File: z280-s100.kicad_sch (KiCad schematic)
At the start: 42 parts, among them J10 Config header (3x8), J7 Serial header (2x5), J8 S-100 edge connector (100-pin), J9 JTAG header (1x6), U1 Z280 Z-BUS (12 MHz), U10 AT28C256 (32Kx8), U11 AT28C256 (32Kx8), U12 LM7805, U13 DS1813, U14 MAX232, U15 74HCT245, U16 74HCT245, U17 74HCT245, U18 74HCT245, U19 74HCT245, U2 74HC573, U20 74HCT245, U21 74HCT244, U22 74F138, U23 74F521, U24 74F521, U25 74F245, U26 74F245, U27 LM323K, U3 74HC573, U4 ATF1508AS (PLCC-84), U5 ATF1508AS (PLCC-84), U6 IS61C5128AS-25QLI (512Kx8), U7 IS61C5128AS-25QLI (512Kx8), U8 IS61C5128AS-25QLI (512Kx8), U9 IS61C5128AS-25QLI (512Kx8), Y1 24 MHz, Y2 24 MHz

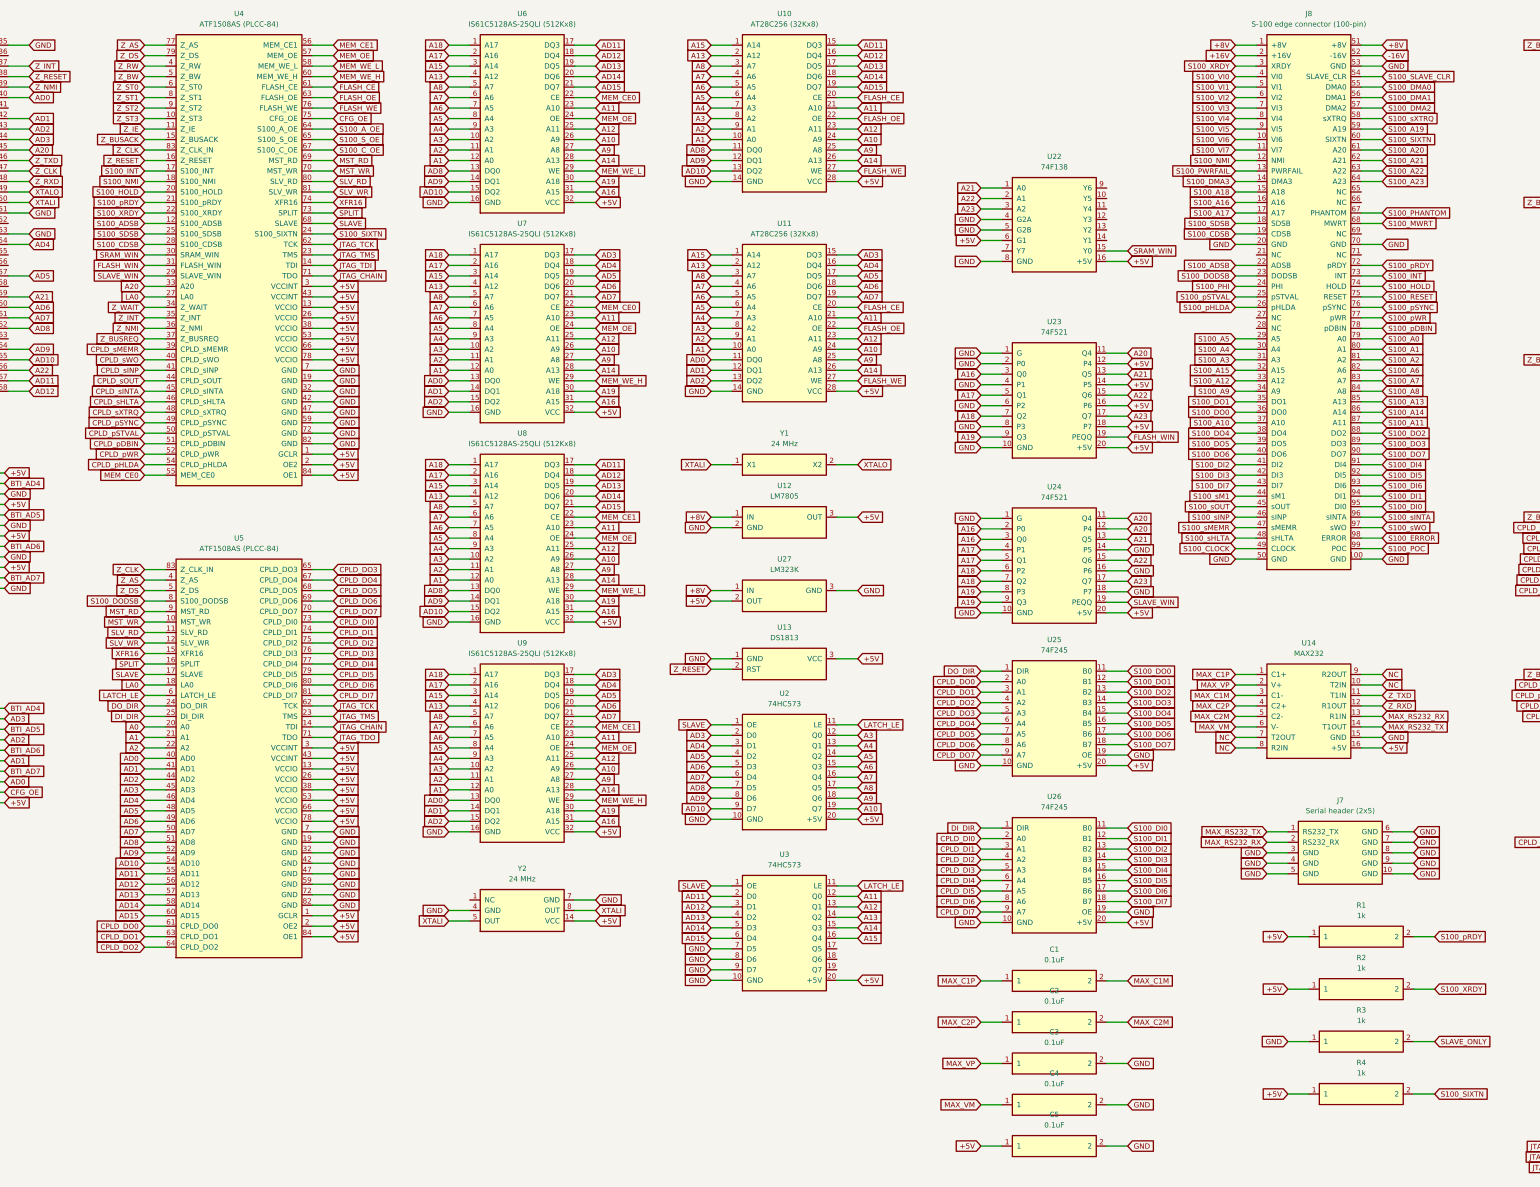
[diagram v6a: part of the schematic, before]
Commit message: Z280 S-100: CPLD pin re-site, SLAVE_ONLY strap, full route + patch area
- Re-pin both CPLDs so signals sit on the package side facing their
  consumers (memory enables up, Z-BUS left, steering right, S-100
  status/control down).
- Restore SLAVE_ONLY debug strap (arbitration: SLAVE = !Z_BUSACK #
  SLAVE_ONLY) + J11 2-pin header + R3 1k pull-down.
- Move interrupts (S100_INT/NMI, Z_INT/Z_NMI) to the data CPLD to free
  control-CPLD pins.
- gen_pcb.py now regenerates the board ab initio: S-100 test-point vias +
  finger traces cloned verbatim, U27 LM323K, +8V island, power planes,
  J11 header, and a 16x10 patch area (PTH sea of holes, 0.1" pitch,
  0.8 mm drills) clear of the DI bus in the upper-right.
- Full FreeRouting pass (2-layer lie workflow, via_costs=15): signal nets
  routed on F.Cu/B.Cu with planes kept off the outer layers; S100_DI2 and
  S100_NMI left hand-routed.

Co-Authored-By: Claude Code <noreply@anthropic.com>
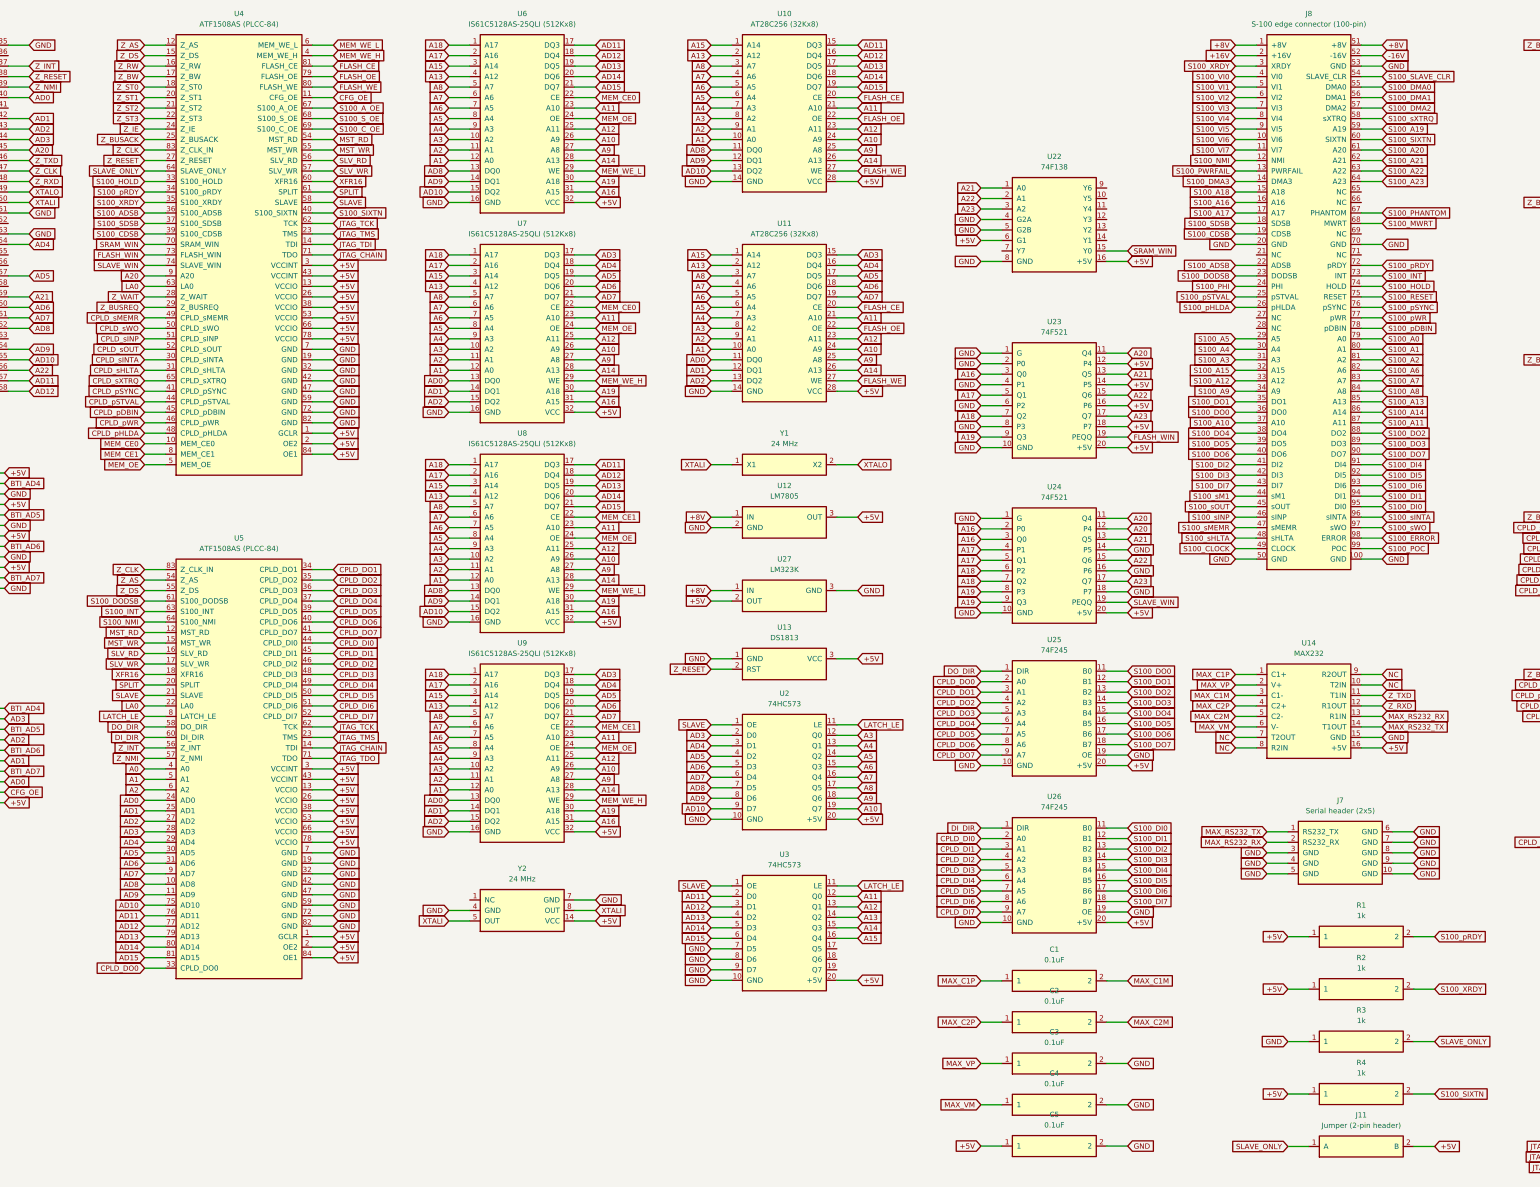
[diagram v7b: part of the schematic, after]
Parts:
- added J11: Jumper (2-pin header), Connector_PinHeader_2.54mm:PinHeader_1x02_P2.54mm_Vertical, symbol z280s100:JP
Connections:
- net +5V: now also J11.2 (B)
- net A0: now also U5.4 (A0); no longer U5.20 (A0)
- net A1: now also U5.5 (A1); no longer U5.21 (A1)
- net A2: now also U5.6 (A2); no longer U5.22 (A2)
- net A20: now also U4.9 (A20); no longer U4.33 (A20)
- net AD0: now also U5.24 (AD0); no longer U5.40 (AD0)
- net AD1: now also U5.25 (AD1); no longer U5.41 (AD1)
- net AD10: now also U5.75 (AD10); no longer U5.54 (AD10)
- net AD11: now also U5.76 (AD11); no longer U5.55 (AD11)
- net AD12: now also U5.77 (AD12); no longer U5.56 (AD12)
- net AD13: now also U5.79 (AD13); no longer U5.57 (AD13)
- net AD14: now also U5.80 (AD14); no longer U5.58 (AD14)
- net AD15: now also U5.81 (AD15); no longer U5.60 (AD15)
- net AD2: now also U5.27 (AD2); no longer U5.44 (AD2)
- net AD3: now also U5.28 (AD3); no longer U5.45 (AD3)
- net AD4: now also U5.29 (AD4); no longer U5.46 (AD4)
- net AD5: now also U5.30 (AD5); no longer U5.48 (AD5)
- net AD6: now also U5.31 (AD6); no longer U5.49 (AD6)
- net AD7: now also U5.9 (AD7); no longer U5.50 (AD7)
- net AD8: now also U5.10 (AD8); no longer U5.51 (AD8)
- net AD9: now also U5.11 (AD9); no longer U5.52 (AD9)
- net CFG_OE: now also U4.11 (CFG_OE); no longer U4.75 (CFG_OE)
- net CPLD_DI0: now also U5.44 (CPLD_DI0); no longer U5.73 (CPLD_DI0)
- net CPLD_DI1: now also U5.45 (CPLD_DI1); no longer U5.74 (CPLD_DI1)
- net CPLD_DI2: now also U5.46 (CPLD_DI2); no longer U5.75 (CPLD_DI2)
- net CPLD_DI3: now also U5.48 (CPLD_DI3); no longer U5.76 (CPLD_DI3)
- net CPLD_DI4: now also U5.49 (CPLD_DI4); no longer U5.77 (CPLD_DI4)
- net CPLD_DI5: now also U5.50 (CPLD_DI5); no longer U5.79 (CPLD_DI5)
- net CPLD_DI6: now also U5.51 (CPLD_DI6); no longer U5.80 (CPLD_DI6)
- net CPLD_DI7: now also U5.52 (CPLD_DI7); no longer U5.81 (CPLD_DI7)
- net CPLD_DO0: now also U5.33 (CPLD_DO0); no longer U5.61 (CPLD_DO0)
- net CPLD_DO1: now also U5.34 (CPLD_DO1); no longer U5.63 (CPLD_DO1)
- net CPLD_DO2: now also U5.35 (CPLD_DO2); no longer U5.64 (CPLD_DO2)
- net CPLD_DO3: now also U5.36 (CPLD_DO3); no longer U5.65 (CPLD_DO3)
- net CPLD_DO4: now also U5.37 (CPLD_DO4); no longer U5.67 (CPLD_DO4)
- net CPLD_DO5: now also U5.39 (CPLD_DO5); no longer U5.68 (CPLD_DO5)
- net CPLD_DO6: now also U5.40 (CPLD_DO6); no longer U5.69 (CPLD_DO6)
- net CPLD_DO7: now also U5.41 (CPLD_DO7); no longer U5.70 (CPLD_DO7)
- net CPLD_pDBIN: now also U4.45 (CPLD_pDBIN); no longer U4.51 (CPLD_pDBIN)
- net CPLD_pHLDA: now also U4.48 (CPLD_pHLDA); no longer U4.54 (CPLD_pHLDA)
- net CPLD_pSTVAL: now also U4.44 (CPLD_pSTVAL); no longer U4.50 (CPLD_pSTVAL)
- net CPLD_pSYNC: now also U4.41 (CPLD_pSYNC); no longer U4.49 (CPLD_pSYNC)
- net CPLD_pWR: now also U4.46 (CPLD_pWR); no longer U4.52 (CPLD_pWR)
- net CPLD_sHLTA: now also U4.31 (CPLD_sHLTA); no longer U4.46 (CPLD_sHLTA)
- net CPLD_sINP: now also U4.51 (CPLD_sINP); no longer U4.41 (CPLD_sINP)
- net CPLD_sINTA: now also U4.30 (CPLD_sINTA); no longer U4.45 (CPLD_sINTA)
- net CPLD_sMEMR: now also U4.49 (CPLD_sMEMR); no longer U4.39 (CPLD_sMEMR)
- net CPLD_sOUT: now also U4.52 (CPLD_sOUT); no longer U4.44 (CPLD_sOUT)
- net CPLD_sWO: now also U4.50 (CPLD_sWO); no longer U4.40 (CPLD_sWO)
- net CPLD_sXTRQ: now also U4.65 (CPLD_sXTRQ); no longer U4.48 (CPLD_sXTRQ)
- net DI_DIR: now also U5.60 (DI_DIR); no longer U5.25 (DI_DIR)
- net DO_DIR: now also U5.58 (DO_DIR); no longer U5.24 (DO_DIR)
- net FLASH_CE: now also U4.81 (FLASH_CE); no longer U4.61 (FLASH_CE)
- net FLASH_OE: now also U4.79 (FLASH_OE); no longer U4.63 (FLASH_OE)
- net FLASH_WE: now also U4.80 (FLASH_WE); no longer U4.76 (FLASH_WE)
- net FLASH_WIN: now also U4.73 (FLASH_WIN); no longer U4.31 (FLASH_WIN)
- net LA0: now also U4.63 (LA0), U5.22 (LA0); no longer U4.27 (LA0), U5.18 (LA0)
- net LATCH_LE: now also U5.8 (LATCH_LE); no longer U5.6 (LATCH_LE)
- net MEM_CE0: now also U4.10 (MEM_CE0); no longer U4.55 (MEM_CE0)
- net MEM_CE1: now also U4.8 (MEM_CE1); no longer U4.56 (MEM_CE1)
- net MEM_OE: now also U4.5 (MEM_OE); no longer U4.57 (MEM_OE)
- net MEM_WE_H: now also U4.4 (MEM_WE_H); no longer U4.60 (MEM_WE_H)
- net MEM_WE_L: now also U4.6 (MEM_WE_L); no longer U4.58 (MEM_WE_L)
- net MST_RD: now also U4.54 (MST_RD), U5.12 (MST_RD); no longer U4.69 (MST_RD), U5.9 (MST_RD)
- net MST_WR: now also U4.55 (MST_WR), U5.15 (MST_WR); no longer U4.70 (MST_WR), U5.10 (MST_WR)
- net S100_ADSB: now also U4.36 (S100_ADSB); no longer U4.12 (S100_ADSB)
- net S100_A_OE: now also U4.67 (S100_A_OE); no longer U4.64 (S100_A_OE)
- net S100_CDSB: now also U4.39 (S100_CDSB); no longer U4.28 (S100_CDSB)
- net S100_C_OE: now also U4.69 (S100_C_OE); no longer U4.67 (S100_C_OE)
- net S100_DODSB: now also U5.61 (S100_DODSB); no longer U5.8 (S100_DODSB)
- net S100_HOLD: now also U4.33 (S100_HOLD); no longer U4.20 (S100_HOLD)
- net S100_INT: now also U5.63 (S100_INT); no longer U4.17 (S100_INT)
- net S100_NMI: now also U5.64 (S100_NMI); no longer U4.18 (S100_NMI)
- net S100_SDSB: now also U4.37 (S100_SDSB); no longer U4.25 (S100_SDSB)
- net S100_SIXTN: now also U4.40 (S100_SIXTN); no longer U4.24 (S100_SIXTN)
- net S100_S_OE: now also U4.68 (S100_S_OE); no longer U4.65 (S100_S_OE)
- net S100_XRDY: now also U4.35 (S100_XRDY); no longer U4.22 (S100_XRDY)
- net S100_pRDY: now also U4.34 (S100_pRDY); no longer U4.21 (S100_pRDY)
- net SLAVE: now also U4.58 (SLAVE), U5.21 (SLAVE); no longer U4.68 (SLAVE), U5.17 (SLAVE)
- net SLAVE_ONLY: now also U4.64 (SLAVE_ONLY), J11.1 (A)
- net SLAVE_WIN: now also U4.74 (SLAVE_WIN); no longer U4.29 (SLAVE_WIN)
- net SLV_RD: now also U4.56 (SLV_RD), U5.16 (SLV_RD); no longer U4.80 (SLV_RD), U5.11 (SLV_RD)
- net SLV_WR: now also U4.57 (SLV_WR), U5.17 (SLV_WR); no longer U4.81 (SLV_WR), U5.12 (SLV_WR)
- net SPLIT: now also U4.61 (SPLIT), U5.20 (SPLIT); no longer U4.73 (SPLIT), U5.16 (SPLIT)
- net SRAM_WIN: now also U4.70 (SRAM_WIN); no longer U4.30 (SRAM_WIN)
- net XFR16: now also U4.60 (XFR16), U5.18 (XFR16); no longer U4.74 (XFR16), U5.15 (XFR16)
- net Z_AS: now also U4.12 (Z_AS), U5.54 (Z_AS); no longer U4.77 (Z_AS), U5.4 (Z_AS)
- net Z_BUSACK: now also U4.25 (Z_BUSACK); no longer U4.15 (Z_BUSACK)
- net Z_BUSREQ: now also U4.29 (Z_BUSREQ); no longer U4.37 (Z_BUSREQ)
- net Z_BW: now also U4.17 (Z_BW); no longer U4.5 (Z_BW)
- net Z_DS: now also U4.15 (Z_DS), U5.55 (Z_DS); no longer U4.79 (Z_DS), U5.5 (Z_DS)
- net Z_IE: now also U4.24 (Z_IE); no longer U4.11 (Z_IE)
- net Z_INT: now also U5.56 (Z_INT); no longer U4.35 (Z_INT)
- net Z_NMI: now also U5.57 (Z_NMI); no longer U4.36 (Z_NMI)
- net Z_RESET: now also U4.27 (Z_RESET); no longer U4.16 (Z_RESET)
- net Z_RW: now also U4.16 (Z_RW); no longer U4.4 (Z_RW)
- net Z_ST0: now also U4.18 (Z_ST0); no longer U4.6 (Z_ST0)
- net Z_ST1: now also U4.20 (Z_ST1); no longer U4.8 (Z_ST1)
- net Z_ST2: now also U4.21 (Z_ST2); no longer U4.9 (Z_ST2)
- net Z_ST3: now also U4.22 (Z_ST3); no longer U4.10 (Z_ST3)
- net Z_WAIT: now also U4.28 (Z_WAIT); no longer U4.34 (Z_WAIT)

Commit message: Z280 S-100: relabel 74F bus parts, silk values, CPLD JEDECs + pin docs
- Address/status/control drivers 74HCT245 -> 74F245; address latch 74HC573 ->
  74F573. 74ACT245/74ACT573 are documented drop-in substitutes at build time
  if the F parts draw too much +5V.
- Move footprint Value from F.Fab to F.SilkS and strip the descriptive
  suffixes so the silkscreen matches the hand-edited board (74F245, 74F573,
  74F138, ...). F.Fab stays a comment-only layer.
- Generate ATF1508 JEDECs for the re-sited CPLDs (ad: 53 MC/3 FF, ctl: 43 MC/7
  FF; pin assignments kept). Document unused I/O for a board rev 2: U5 has
  65/67/68/69/70/73/74 free, U4 has 75/76/77 free + Z_AS (pin 12) as a spare.

Co-Authored-By: Claude Code <noreply@anthropic.com>
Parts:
- U15, U16, U17, U18, U19, U20: value 74HCT245 -> 74F245; symbol z280s100:74HCT245 -> z280s100:74F245
- U2, U3: value 74HC573 -> 74F573; symbol z280s100:74HC573 -> z280s100:74F573
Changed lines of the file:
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@@
     (property "Intersheetrefs" "${INTERSHEET_REFS}" (at 0 0 0) (effects (font (size 1.27 1.27)) hide))
   )
-  (symbol (lib_id "z280s100:74HC573")
+  (symbol (lib_id "z280s100:74F573")
     (at 294.64 190.00 0)
     (unit 1) (exclude_from_sim no) (in_bom yes) (on_board yes) (dnp no) (fields_autoplaced yes)
     (property "Reference" "U2" (at 294.64 182.38 0) (effects (font (size 1.27 1.27))))
-    (property "Value" "74HC573" (at 294.64 184.92 0) (effects (font (size 1.27 1.27))))
+    (property "Value" "74F573" (at 294.64 184.92 0) (effects (font (size 1.27 1.27))))
     (property "Footprint" "Package_DIP:DIP-20_W7.62mm" (at 294.64 190.00 0) (effects (font (size 1.27 1.27)) hide))
     (property "Datasheet" "" (at 0 0 0) (effects (font (size 1.27 1.27)) hide))
@@
     (property "Intersheetrefs" "${INTERSHEET_REFS}" (at 0 0 0) (effects (font (size 1.27 1.27)) hide))
   )
-  (symbol (lib_id "z280s100:74HC573")
+  (symbol (lib_id "z280s100:74F573")
     (at 294.64 229.00 0)
     (unit 1) (exclude_from_sim no) (in_bom yes) (on_board yes) (dnp no) (fields_autoplaced yes)
     (property "Reference" "U3" (at 294.64 221.38 0) (effects (font (size 1.27 1.27))))
-    (property "Value" "74HC573" (at 294.64 223.92 0) (effects (font (size 1.27 1.27))))
+    (property "Value" "74F573" (at 294.64 223.92 0) (effects (font (size 1.27 1.27))))
     (property "Footprint" "Package_DIP:DIP-20_W7.62mm" (at 294.64 229.00 0) (effects (font (size 1.27 1.27)) hide))
     (property "Datasheet" "" (at 0 0 0) (effects (font (size 1.27 1.27)) hide))
@@
     (property "Intersheetrefs" "${INTERSHEET_REFS}" (at 0 0 0) (effects (font (size 1.27 1.27)) hide))
   )
-  (symbol (lib_id "z280s100:74HCT245")
+  (symbol (lib_id "z280s100:74F245")
     (at 502.92 25.40 0)
     (unit 1) (exclude_from_sim no) (in_bom yes) (on_board yes) (dnp no) (fields_autoplaced yes)
     (property "Reference" "U15" (at 502.92 17.78 0) (effects (font (size 1.27 1.27))))
-    (property "Value" "74HCT245" (at 502.92 20.32 0) (effects (font (size 1.27 1.27))))
+    (property "Value" "74F245" (at 502.92 20.32 0) (effects (font (size 1.27 1.27))))
     (property "Footprint" "Package_DIP:DIP-20_W7.62mm" (at 502.92 25.40 0) (effects (font (size 1.27 1.27)) hide))
     (property "Datasheet" "" (at 0 0 0) (effects (font (size 1.27 1.27)) hide))
@@
     (property "Intersheetrefs" "${INTERSHEET_REFS}" (at 0 0 0) (effects (font (size 1.27 1.27)) hide))
   )
-  (symbol (lib_id "z280s100:74HCT245")
+  (symbol (lib_id "z280s100:74F245")
     (at 502.92 63.50 0)
     (unit 1) (exclude_from_sim no) (in_bom yes) (on_board yes) (dnp no) (fields_autoplaced yes)
     (property "Reference" "U16" (at 502.92 55.88 0) (effects (font (size 1.27 1.27))))
-    (property "Value" "74HCT245" (at 502.92 58.42 0) (effects (font (size 1.27 1.27))))
+    (property "Value" "74F245" (at 502.92 58.42 0) (effects (font (size 1.27 1.27))))
     (property "Footprint" "Package_DIP:DIP-20_W7.62mm" (at 502.92 63.50 0) (effects (font (size 1.27 1.27)) hide))
     (property "Datasheet" "" (at 0 0 0) (effects (font (size 1.27 1.27)) hide))
@@
     (property "Intersheetrefs" "${INTERSHEET_REFS}" (at 0 0 0) (effects (font (size 1.27 1.27)) hide))
   )
-  (symbol (lib_id "z280s100:74HCT245")
+  (symbol (lib_id "z280s100:74F245")
     (at 502.92 101.60 0)
     (unit 1) (exclude_from_sim no) (in_bom yes) (on_board yes) (dnp no) (fields_autoplaced yes)
     (property "Reference" "U17" (at 502.92 93.98 0) (effects (font (size 1.27 1.27))))
-    (property "Value" "74HCT245" (at 502.92 96.52 0) (effects (font (size 1.27 1.27))))
+    (property "Value" "74F245" (at 502.92 96.52 0) (effects (font (size 1.27 1.27))))
     (property "Footprint" "Package_DIP:DIP-20_W7.62mm" (at 502.92 101.60 0) (effects (font (size 1.27 1.27)) hide))
     (property "Datasheet" "" (at 0 0 0) (effects (font (size 1.27 1.27)) hide))
@@
     (property "Intersheetrefs" "${INTERSHEET_REFS}" (at 0 0 0) (effects (font (size 1.27 1.27)) hide))
   )
-  (symbol (lib_id "z280s100:74HCT245")
+  (symbol (lib_id "z280s100:74F245")
     (at 502.92 139.70 0)
     (unit 1) (exclude_from_sim no) (in_bom yes) (on_board yes) (dnp no) (fields_autoplaced yes)
     (property "Reference" "U18" (at 502.92 132.08 0) (effects (font (size 1.27 1.27))))
-    (property "Value" "74HCT245" (at 502.92 134.62 0) (effects (font (size 1.27 1.27))))
+    (property "Value" "74F245" (at 502.92 134.62 0) (effects (font (size 1.27 1.27))))
     (property "Footprint" "Package_DIP:DIP-20_W7.62mm" (at 502.92 139.70 0) (effects (font (size 1.27 1.27)) hide))
     (property "Datasheet" "" (at 0 0 0) (effects (font (size 1.27 1.27)) hide))
@@
     (property "Intersheetrefs" "${INTERSHEET_REFS}" (at 0 0 0) (effects (font (size 1.27 1.27)) hide))
   )
-  (symbol (lib_id "z280s100:74HCT245")
+  (symbol (lib_id "z280s100:74F245")
     (at 502.92 177.80 0)
     (unit 1) (exclude_from_sim no) (in_bom yes) (on_board yes) (dnp no) (fields_autoplaced yes)
     (property "Reference" "U19" (at 502.92 170.18 0) (effects (font (size 1.27 1.27))))
-    (property "Value" "74HCT245" (at 502.92 172.72 0) (effects (font (size 1.27 1.27))))
+    (property "Value" "74F245" (at 502.92 172.72 0) (effects (font (size 1.27 1.27))))
     (property "Footprint" "Package_DIP:DIP-20_W7.62mm" (at 502.92 177.80 0) (effects (font (size 1.27 1.27)) hide))
     (property "Datasheet" "" (at 0 0 0) (effects (font (size 1.27 1.27)) hide))
@@
     (property "Intersheetrefs" "${INTERSHEET_REFS}" (at 0 0 0) (effects (font (size 1.27 1.27)) hide))
   )
-  (symbol (lib_id "z280s100:74HCT245")
+  (symbol (lib_id "z280s100:74F245")
     (at 502.92 215.90 0)
     (unit 1) (exclude_from_sim no) (in_bom yes) (on_board yes) (dnp no) (fields_autoplaced yes)
     (property "Reference" "U20" (at 502.92 208.28 0) (effects (font (size 1.27 1.27))))
-    (property "Value" "74HCT245" (at 502.92 210.82 0) (effects (font (size 1.27 1.27))))
+    (property "Value" "74F245" (at 502.92 210.82 0) (effects (font (size 1.27 1.27))))
     (property "Footprint" "Package_DIP:DIP-20_W7.62mm" (at 502.92 215.90 0) (effects (font (size 1.27 1.27)) hide))
     (property "Datasheet" "" (at 0 0 0) (effects (font (size 1.27 1.27)) hide))
